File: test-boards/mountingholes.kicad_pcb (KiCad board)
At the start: 2 copper layers, 120 x 120 mm, 7 parts

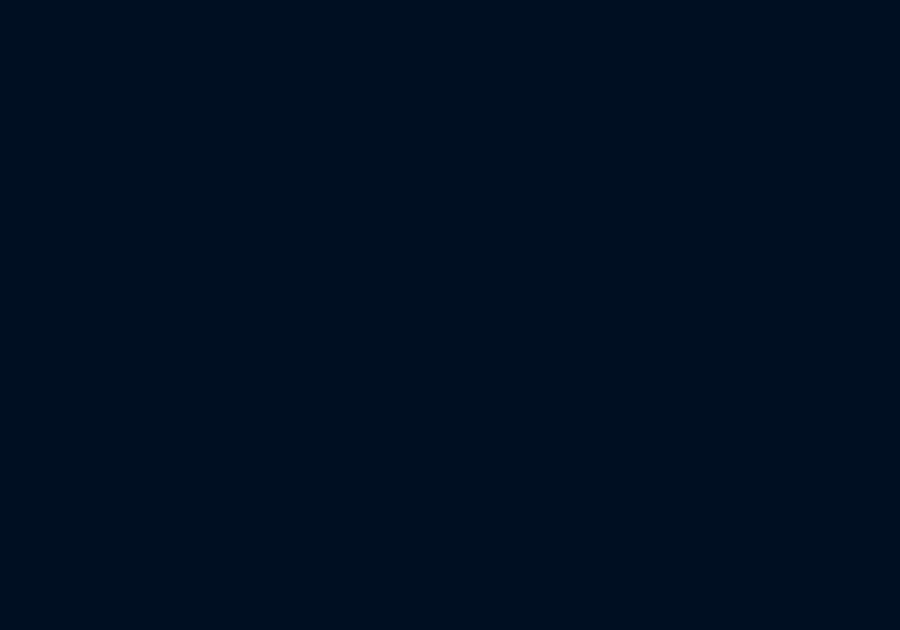
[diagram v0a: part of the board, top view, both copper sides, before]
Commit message: We got the basic box working using templates
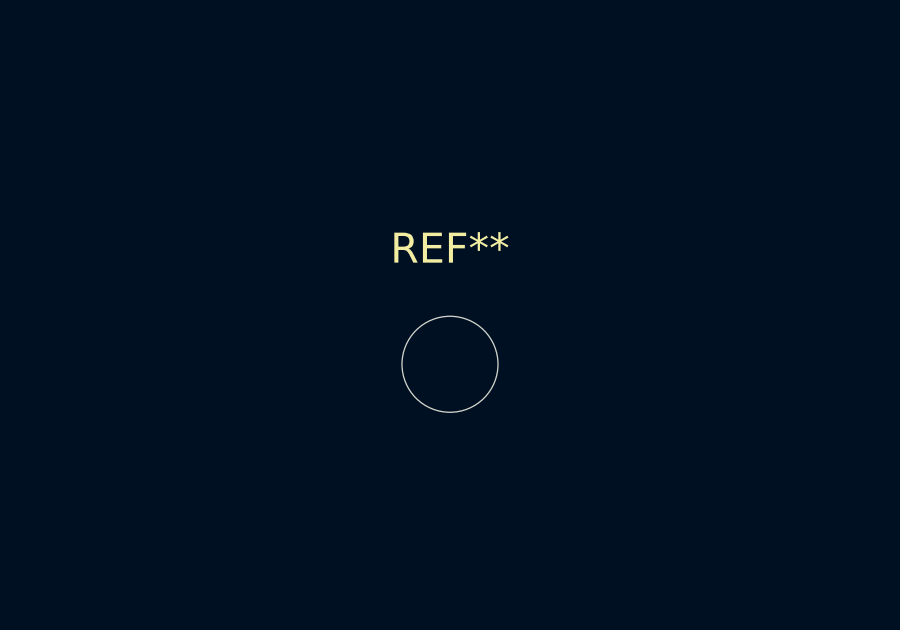
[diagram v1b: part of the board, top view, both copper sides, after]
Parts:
- added REF**: MountingHole_3.2mm_M3_ISO7380, MountingHole:MountingHole_3.2mm_M3_ISO7380, F.Cu at (123.5, 71.5)
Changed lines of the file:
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@@
 				(font
 					(size 1.27 1.27)
+					(thickness 0.15)
 				)
 			)
@@
 				(font
 					(size 1.27 1.27)
+					(thickness 0.15)
 				)
 			)
@@
 				(font
 					(size 1.27 1.27)
+					(thickness 0.15)
 				)
 			)
@@
 				(font
 					(size 1.27 1.27)
+					(thickness 0.15)
 				)
 			)
@@
 				(font
 					(size 1.27 1.27)
+					(thickness 0.15)
 				)
 			)
@@
 				(font
 					(size 1.27 1.27)
+					(thickness 0.15)
 				)
 			)
@@
 				(font
 					(size 1.27 1.27)
+					(thickness 0.15)
 				)
 			)
@@
 				(font
 					(size 1.27 1.27)
+					(thickness 0.15)
 				)
 			)
@@
 				(font
 					(size 1.27 1.27)
+					(thickness 0.15)
 				)
 			)
@@
 				(font
 					(size 1.27 1.27)
+					(thickness 0.15)
 				)
 			)
@@
 				(font
 					(size 1.27 1.27)
+					(thickness 0.15)
 				)
 			)
@@
 				(font
 					(size 1.27 1.27)
+					(thickness 0.15)
 				)
 			)
@@
 				(font
 					(size 1.27 1.27)
+					(thickness 0.15)
 				)
 			)
@@
 				(font
 					(size 1.27 1.27)
+					(thickness 0.15)
 				)
 			)
@@
 				(font
 					(size 1.27 1.27)
+					(thickness 0.15)
 				)
 			)
@@
 			(size 6.4 6.4)
 			(drill 6.4)
+			(layers "*.Cu" "*.Mask")
+		)
+	)
+	(footprint "MountingHole:MountingHole_3.2mm_M3_ISO7380"
+		(layer "F.Cu")
+		(at 123.5 71.5)
+		(descr "Mounting Hole 3.2mm, no annular, M3, ISO7380")
+		(tags "mounting hole 3.2mm no annular m3 iso7380")
+		(property "Reference" "REF**"
+			(at 0 -3.85 0)
+			(layer "F.SilkS")
+			(effects
+				(font
+					(size 1 1)
+					(thickness 0.15)
+				)
+			)
+		)
+		(property "Value" "MountingHole_3.2mm_M3_ISO7380"
+			(at 0 3.85 0)
+			(layer "F.Fab")
+			(effects
+				(font
+					(size 1 1)
+					(thickness 0.15)
+				)
+			)
+		)
+		(property "Footprint" "MountingHole:MountingHole_3.2mm_M3_ISO7380"
+			(at 0 0 0)
+			(layer "F.Fab")
+			(hide yes)
+			(effects
+				(font
+					(size 1.27 1.27)
+					(thickness 0.15)
+				)
+			)
+		)
+		(property "Datasheet" ""
+			(at 0 0 0)
+			(layer "F.Fab")
+			(hide yes)
+			(effects
+				(font
+					(size 1.27 1.27)
+					(thickness 0.15)
+				)
+			)
+		)
+		(property "Description" ""
+			(at 0 0 0)
+			(layer "F.Fab")
+			(hide yes)
+			(effects
+				(font
+					(size 1.27 1.27)
+					(thickness 0.15)
+				)
+			)
+		)
+		(attr exclude_from_pos_files exclude_from_bom)
+		(fp_circle
+			(center 0 0)
+			(end 2.85 0)
+			(stroke
+				(width 0.15)
+				(type solid)
+			)
+			(fill none)
+			(layer "Cmts.User")
+		)
+		(fp_circle
+			(center 0 0)
+			(end 3.1 0)
+			(stroke
+				(width 0.05)
+				(type solid)
+			)
+			(fill none)
+			(layer "F.CrtYd")
+		)
+		(fp_text user "${REFERENCE}"
+			(at 0 0 0)
+			(layer "F.Fab")
+			(effects
+				(font
+					(size 1 1)
+					(thickness 0.15)
+				)
+			)
+		)
+		(pad "" np_thru_hole circle
+			(at 0 0)
+			(size 3.2 3.2)
+			(drill 3.2)
 			(layers "*.Cu" "*.Mask")
 		)
@@
 				(font
 					(size 1.27 1.27)
+					(thickness 0.15)
 				)
 			)
@@
 				(font
 					(size 1.27 1.27)
+					(thickness 0.15)
 				)
 			)
@@
 				(font
 					(size 1.27 1.27)
+					(thickness 0.15)
 				)
 			)
@@
 				(font
 					(size 1.27 1.27)
+					(thickness 0.15)
 				)
 			)
@@
 				(font
 					(size 1.27 1.27)
+					(thickness 0.15)
 				)
 			)
@@
 				(font
 					(size 1.27 1.27)
+					(thickness 0.15)
 				)
 			)
@@
 	(gr_circle
 		(center 100 100)
-		(end 161 100)
+		(end 162.5 95.5)
 		(stroke
 			(width 0.15)

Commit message: Reset mounting holes board
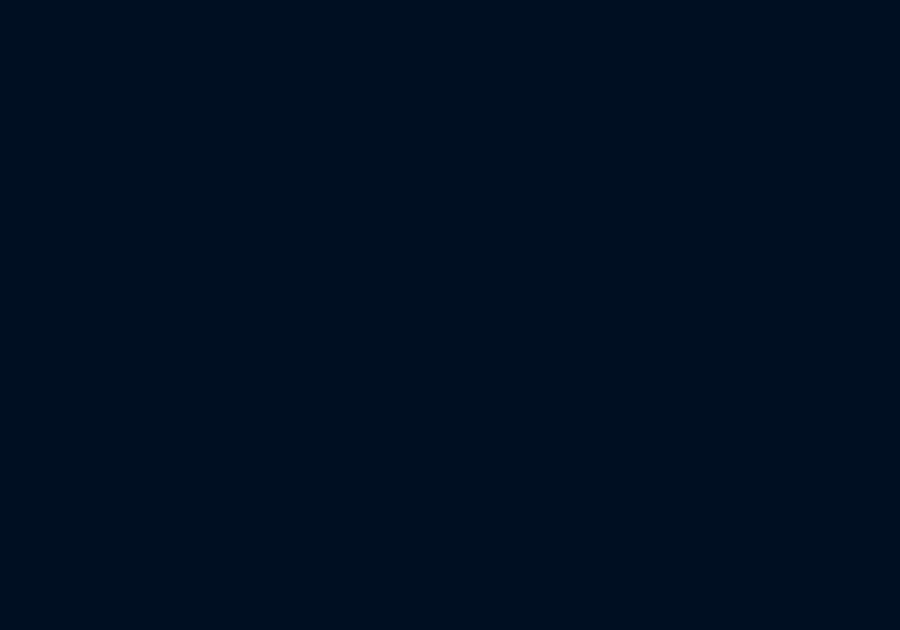
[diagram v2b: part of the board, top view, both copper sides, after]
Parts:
- removed the REF** at (123.5, 71.5)
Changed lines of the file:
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@@
 				(font
 					(size 1.27 1.27)
-					(thickness 0.15)
 				)
 			)
@@
 				(font
 					(size 1.27 1.27)
-					(thickness 0.15)
 				)
 			)
@@
 				(font
 					(size 1.27 1.27)
-					(thickness 0.15)
 				)
 			)
@@
 				(font
 					(size 1.27 1.27)
-					(thickness 0.15)
 				)
 			)
@@
 				(font
 					(size 1.27 1.27)
-					(thickness 0.15)
 				)
 			)
@@
 				(font
 					(size 1.27 1.27)
-					(thickness 0.15)
 				)
 			)
@@
 				(font
 					(size 1.27 1.27)
-					(thickness 0.15)
 				)
 			)
@@
 				(font
 					(size 1.27 1.27)
-					(thickness 0.15)
 				)
 			)
@@
 				(font
 					(size 1.27 1.27)
-					(thickness 0.15)
 				)
 			)
@@
 				(font
 					(size 1.27 1.27)
-					(thickness 0.15)
 				)
 			)
@@
 				(font
 					(size 1.27 1.27)
-					(thickness 0.15)
 				)
 			)
@@
 				(font
 					(size 1.27 1.27)
-					(thickness 0.15)
 				)
 			)
@@
 				(font
 					(size 1.27 1.27)
-					(thickness 0.15)
 				)
 			)
@@
 				(font
 					(size 1.27 1.27)
-					(thickness 0.15)
 				)
 			)
@@
 				(font
 					(size 1.27 1.27)
-					(thickness 0.15)
 				)
 			)
@@
 			(size 6.4 6.4)
 			(drill 6.4)
-			(layers "*.Cu" "*.Mask")
-		)
-	)
-	(footprint "MountingHole:MountingHole_3.2mm_M3_ISO7380"
-		(layer "F.Cu")
-		(at 123.5 71.5)
-		(descr "Mounting Hole 3.2mm, no annular, M3, ISO7380")
-		(tags "mounting hole 3.2mm no annular m3 iso7380")
-		(property "Reference" "REF**"
-			(at 0 -3.85 0)
-			(layer "F.SilkS")
-			(effects
-				(font
-					(size 1 1)
-					(thickness 0.15)
-				)
-			)
-		)
-		(property "Value" "MountingHole_3.2mm_M3_ISO7380"
-			(at 0 3.85 0)
-			(layer "F.Fab")
-			(effects
-				(font
-					(size 1 1)
-					(thickness 0.15)
-				)
-			)
-		)
-		(property "Footprint" "MountingHole:MountingHole_3.2mm_M3_ISO7380"
-			(at 0 0 0)
-			(layer "F.Fab")
-			(hide yes)
-			(effects
-				(font
-					(size 1.27 1.27)
-					(thickness 0.15)
-				)
-			)
-		)
-		(property "Datasheet" ""
-			(at 0 0 0)
-			(layer "F.Fab")
-			(hide yes)
-			(effects
-				(font
-					(size 1.27 1.27)
-					(thickness 0.15)
-				)
-			)
-		)
-		(property "Description" ""
-			(at 0 0 0)
-			(layer "F.Fab")
-			(hide yes)
-			(effects
-				(font
-					(size 1.27 1.27)
-					(thickness 0.15)
-				)
-			)
-		)
-		(attr exclude_from_pos_files exclude_from_bom)
-		(fp_circle
-			(center 0 0)
-			(end 2.85 0)
-			(stroke
-				(width 0.15)
-				(type solid)
-			)
-			(fill none)
-			(layer "Cmts.User")
-		)
-		(fp_circle
-			(center 0 0)
-			(end 3.1 0)
-			(stroke
-				(width 0.05)
-				(type solid)
-			)
-			(fill none)
-			(layer "F.CrtYd")
-		)
-		(fp_text user "${REFERENCE}"
-			(at 0 0 0)
-			(layer "F.Fab")
-			(effects
-				(font
-					(size 1 1)
-					(thickness 0.15)
-				)
-			)
-		)
-		(pad "" np_thru_hole circle
-			(at 0 0)
-			(size 3.2 3.2)
-			(drill 3.2)
 			(layers "*.Cu" "*.Mask")
 		)
@@
 				(font
 					(size 1.27 1.27)
-					(thickness 0.15)
 				)
 			)
@@
 				(font
 					(size 1.27 1.27)
-					(thickness 0.15)
 				)
 			)
@@
 				(font
 					(size 1.27 1.27)
-					(thickness 0.15)
 				)
 			)
@@
 				(font
 					(size 1.27 1.27)
-					(thickness 0.15)
 				)
 			)
@@
 				(font
 					(size 1.27 1.27)
-					(thickness 0.15)
 				)
 			)
@@
 				(font
 					(size 1.27 1.27)
-					(thickness 0.15)
 				)
 			)
@@
 	(gr_circle
 		(center 100 100)
-		(end 162.5 95.5)
+		(end 161 100)
 		(stroke
 			(width 0.15)
